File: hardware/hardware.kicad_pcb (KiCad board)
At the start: 2 copper layers, 39 parts, among them J1 USB_C_Receptacle_USB2.0, J2 Conn_01x12_Pin, J4 Conn_01x12_Pin, SW1 RST, SW2 BOOT, U1 ESP32-C3-MINI-1, U2 CH217K, U3 AMS1117-3.3, U4 DHT11, U5 BMP280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

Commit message: PCB is ready for print.
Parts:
- moved U4 54.3 mm to (145.4, 87.5), turned to 90 degrees
- moved U6 48.1 mm to (157.9, 75.5), turned to 0 degrees
- moved D3 47.0 mm to (159.0, 87.3)
- moved R11 41.8 mm to (155.0, 78.5)
- moved C7 38.9 mm to (164.0, 70.0)
- moved R18 37.4 mm to (163.7, 84.1)
- moved R17 36.0 mm to (163.7, 79.0)
- moved R16 32.8 mm to (163.7, 73.9)
- moved SW2 28.3 mm to (187.1, 68.1)
- moved D1 27.4 mm to (149.6, 65.2)
- moved U3 25.4 mm to (139.0, 65.5)
- moved C4 24.5 mm to (169.5, 68.5)
- moved R7 20.0 mm to (168.5, 74.4), turned to 0 degrees
- moved C1 18.9 mm to (155.5, 63.0)
- moved C3 18.7 mm to (173.5, 66.9)
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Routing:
- net GND: track 263.9 -> 72.4 mm, vias 0 -> 67
- net IO9_BOOT: track 88.3 -> 43.3 mm, vias 2 -> 1
- net IO3_SDA: track 122.5 -> 81.4 mm
- net IO2: track 46.7 -> 82.6 mm, vias 1 -> 3
- net IO8: track 67.4 -> 49.1 mm, vias 2 -> 0
- net 3V3: track 234.0 -> 215.8 mm, vias 1 -> 0
- net Net-(U2-VIN): track 18.5 -> 36.6 mm, vias 3 -> 0
- net IO10: track 32.9 -> 49.9 mm
- net IO5: track 34.7 -> 18.4 mm, vias 2 -> 0
- net IO18: track 39.9 -> 56.0 mm, vias 1 -> 2
- net Net-(D3-A): track 24.3 -> 10.1 mm, vias 0 -> 1
- net USBD-: track 14.6 -> 26.1 mm, vias 2 -> 0
- net Net-(J1-CC2): track 3.24 -> 13.0 mm
- net IO7: track 22.0 -> 12.3 mm, vias 1 -> 0
- net IO19: track 46.9 -> 56.5 mm, vias 1 -> 2
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- added copper zone on B.Cu, net GND
- added copper zone on F.Cu, net GND
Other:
- board outline added: 65.5 x 31 mm

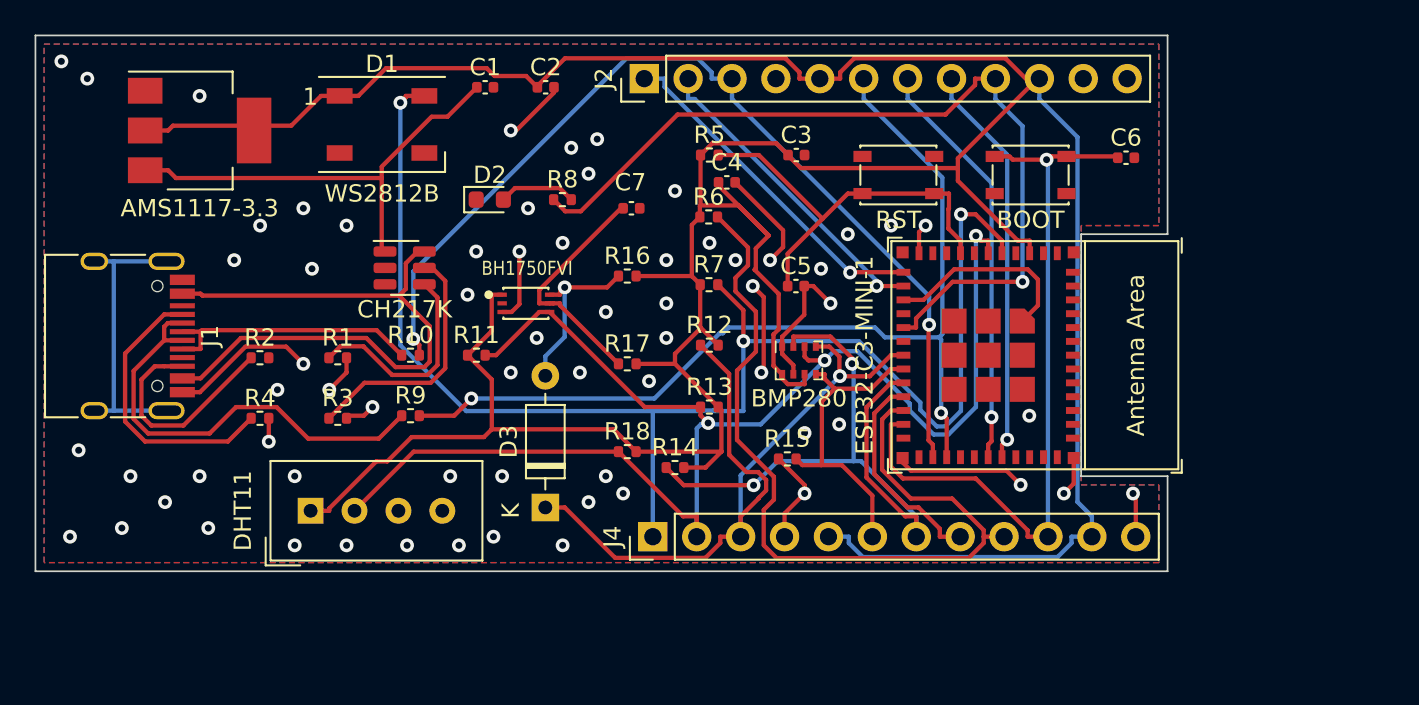
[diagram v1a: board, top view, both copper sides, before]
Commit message: Draft version to enable stepper.
And have some changes on KiCad data, may have something wrong. Let's just keep them now.
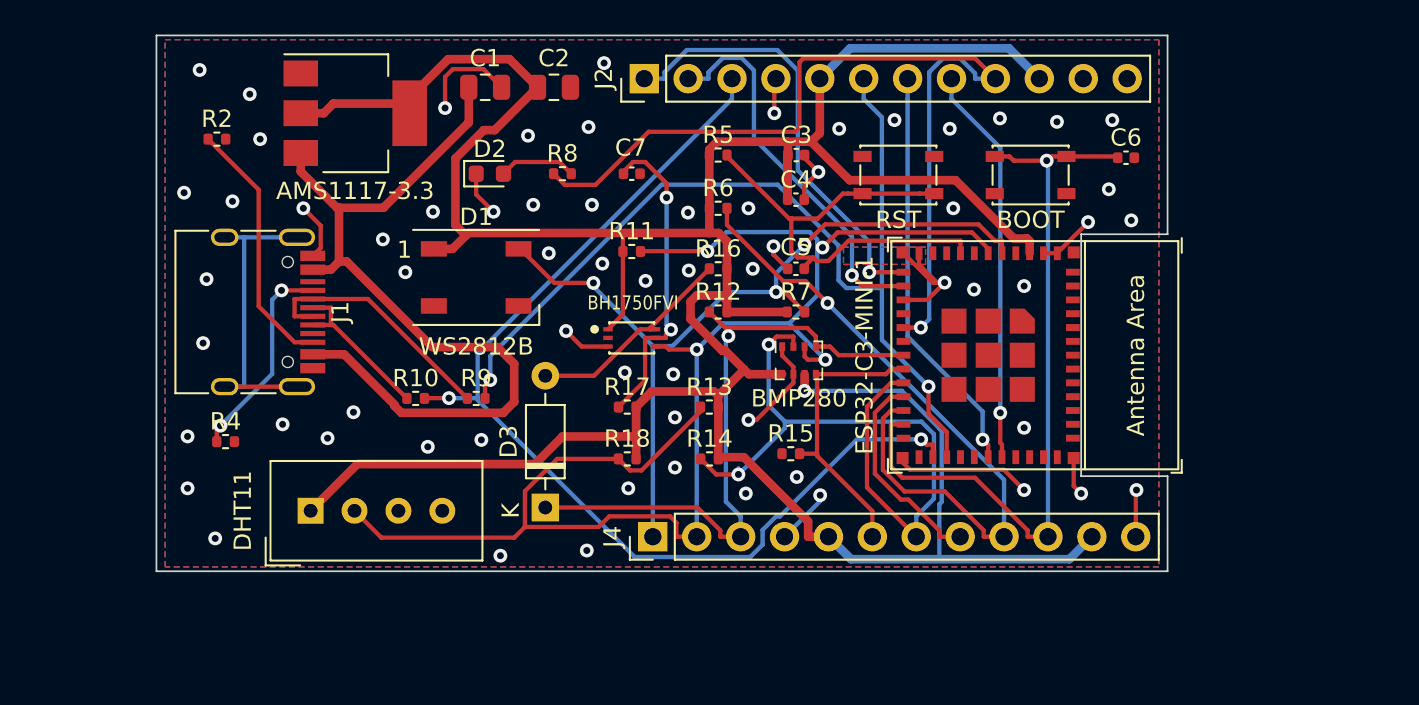
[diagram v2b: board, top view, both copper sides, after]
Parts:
- removed R1: 10K, Resistor_SMD:R_0402_1005Metric
- removed R3: 56K, Resistor_SMD:R_0402_1005Metric
- removed U2: CH217K, Package_TO_SOT_SMD:SOT-23-6
- C1, C2: footprint Capacitor_SMD:C_0402_1005Metric -> Capacitor_SMD:C_0805_2012Metric
- C7: value 0.1uF -> 100nF
- moved R2 12.9 mm to (140.0, 66.0)
- moved R11 10.8 mm to (164.0, 72.5)
- moved D1 10.4 mm to (155.0, 74.0)
- moved U3 9.06 mm to (148.0, 64.5)
- moved J1 7.67 mm to (141.5, 76.0)
- moved U6 6.44 mm to (164.0, 77.5)
- moved R16 5.28 mm to (169.0, 73.5)
- moved R7 5.27 mm to (173.5, 76.0)
- moved C4 4.12 mm to (173.5, 69.5)
- moved R9 3.93 mm to (155.0, 81.0)
- moved R10 2.52 mm to (151.5, 81.0)
- moved R17 2.50 mm to (163.7, 81.5)
- moved R4 2.40 mm to (140.5, 83.5)
- moved R14 2.06 mm to (168.5, 84.5)
- moved C7 2.00 mm to (164.0, 68.0)
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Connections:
- J1 pad A4: Net-(U2-VIN) -> +5V
- J1 pad A9: Net-(U2-VIN) -> +5V
- J1 pad B4: Net-(U2-VIN) -> +5V
- J1 pad B9: Net-(U2-VIN) -> +5V
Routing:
- net Net-(U2-VIN): track 36.6 -> 0.00 mm
- net IO2: track 82.6 -> 48.3 mm
- net +5V: track 26.3 -> 48.7 mm
- net 3V3: track 215.8 -> 197.0 mm, vias 0 -> 1
- net GND: track 72.4 -> 55.4 mm, vias 67 -> 65
- net Net-(U2-ISET): track 14.5 -> 0.00 mm
- net Net-(U2-EN#): track 12.5 -> 0.00 mm
- net USBD-: track 26.1 -> 14.4 mm
- net IO8: track 49.1 -> 39.6 mm, vias 0 -> 1
- net IO4_SCL: track 45.5 -> 37.3 mm
- net IO3_SDA: track 81.4 -> 88.2 mm, vias 3 -> 4
- net USBD+: track 15.4 -> 9.26 mm
- net IO18: track 56.0 -> 62.0 mm
- net IO0: track 19.9 -> 25.6 mm
- net Net-(U6-DVI): track 13.7 -> 18.4 mm, vias 0 -> 2
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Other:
- board size 65.5 x 31 mm -> 58.5 x 31 mm
